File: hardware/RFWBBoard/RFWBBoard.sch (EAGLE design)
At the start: 8 parts, among them J1 CON-71742-2184-BOT, M1 MOUNT-HOLE3.3, M2 MOUNT-HOLE3.3, M3 MOUNT-HOLE3.3, M4 MOUNT-HOLE3.3, U1 MAX2830, U2 LDB212G4010C-001, U3 LDB212G4010C-001

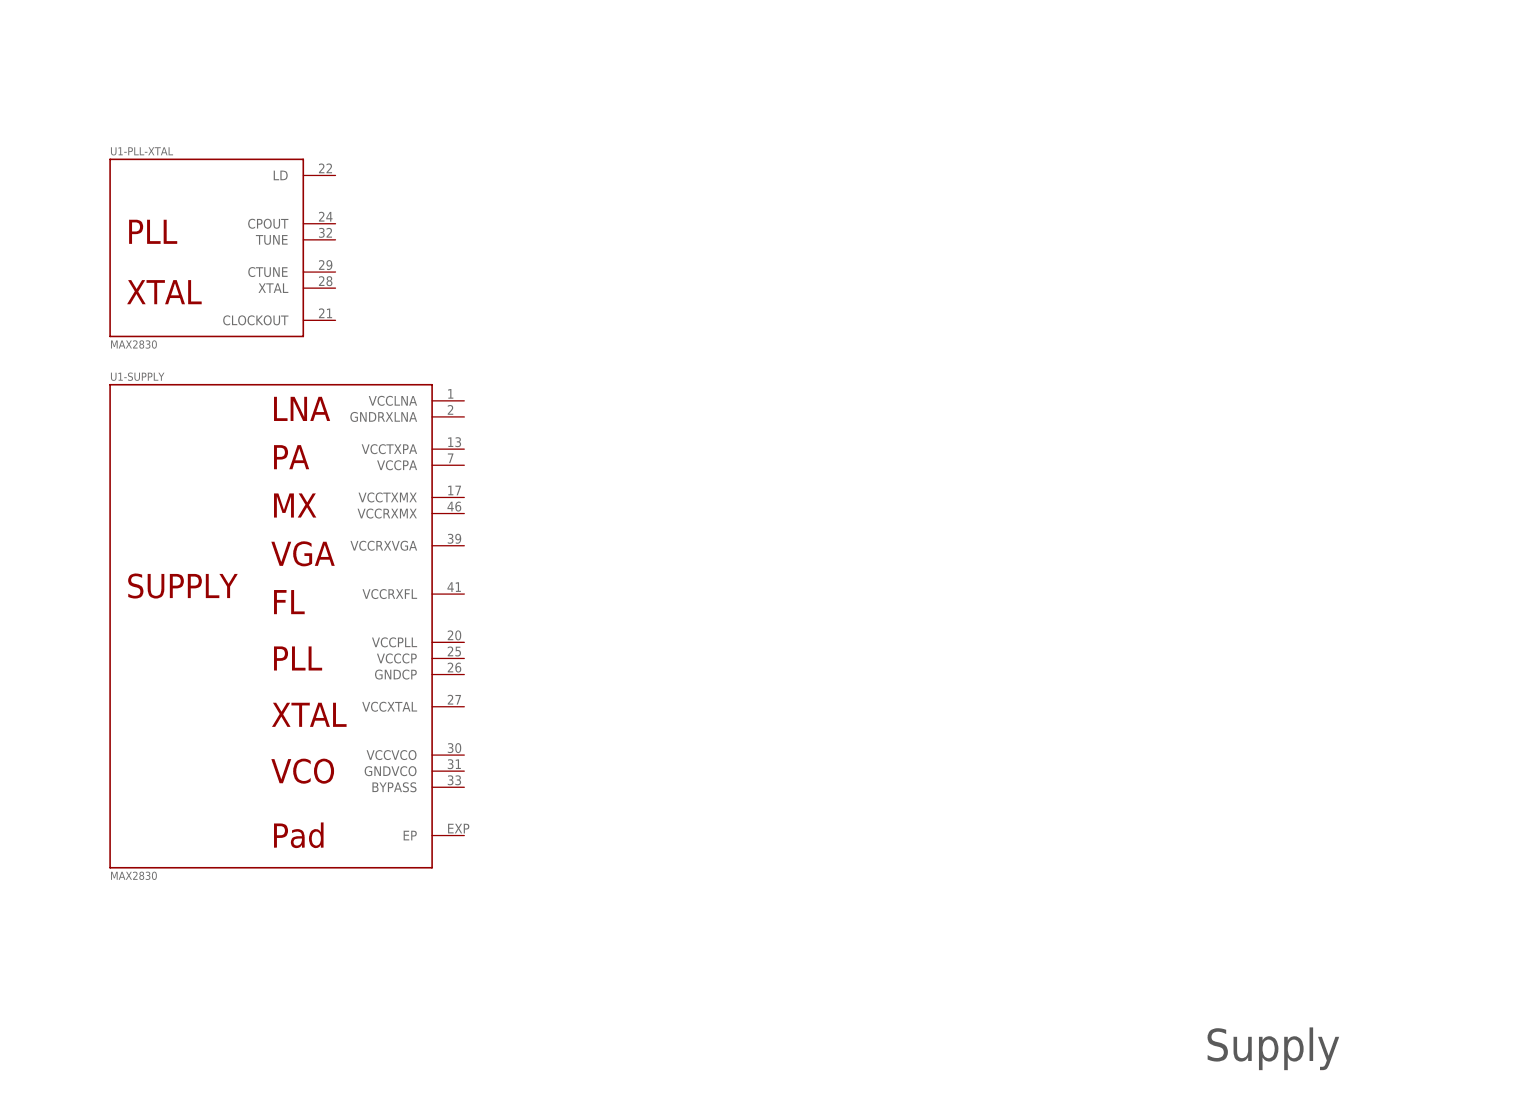
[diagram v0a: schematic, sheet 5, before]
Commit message: - 2.4 GHz Wide-Band Radio Front-End Board has most of the components
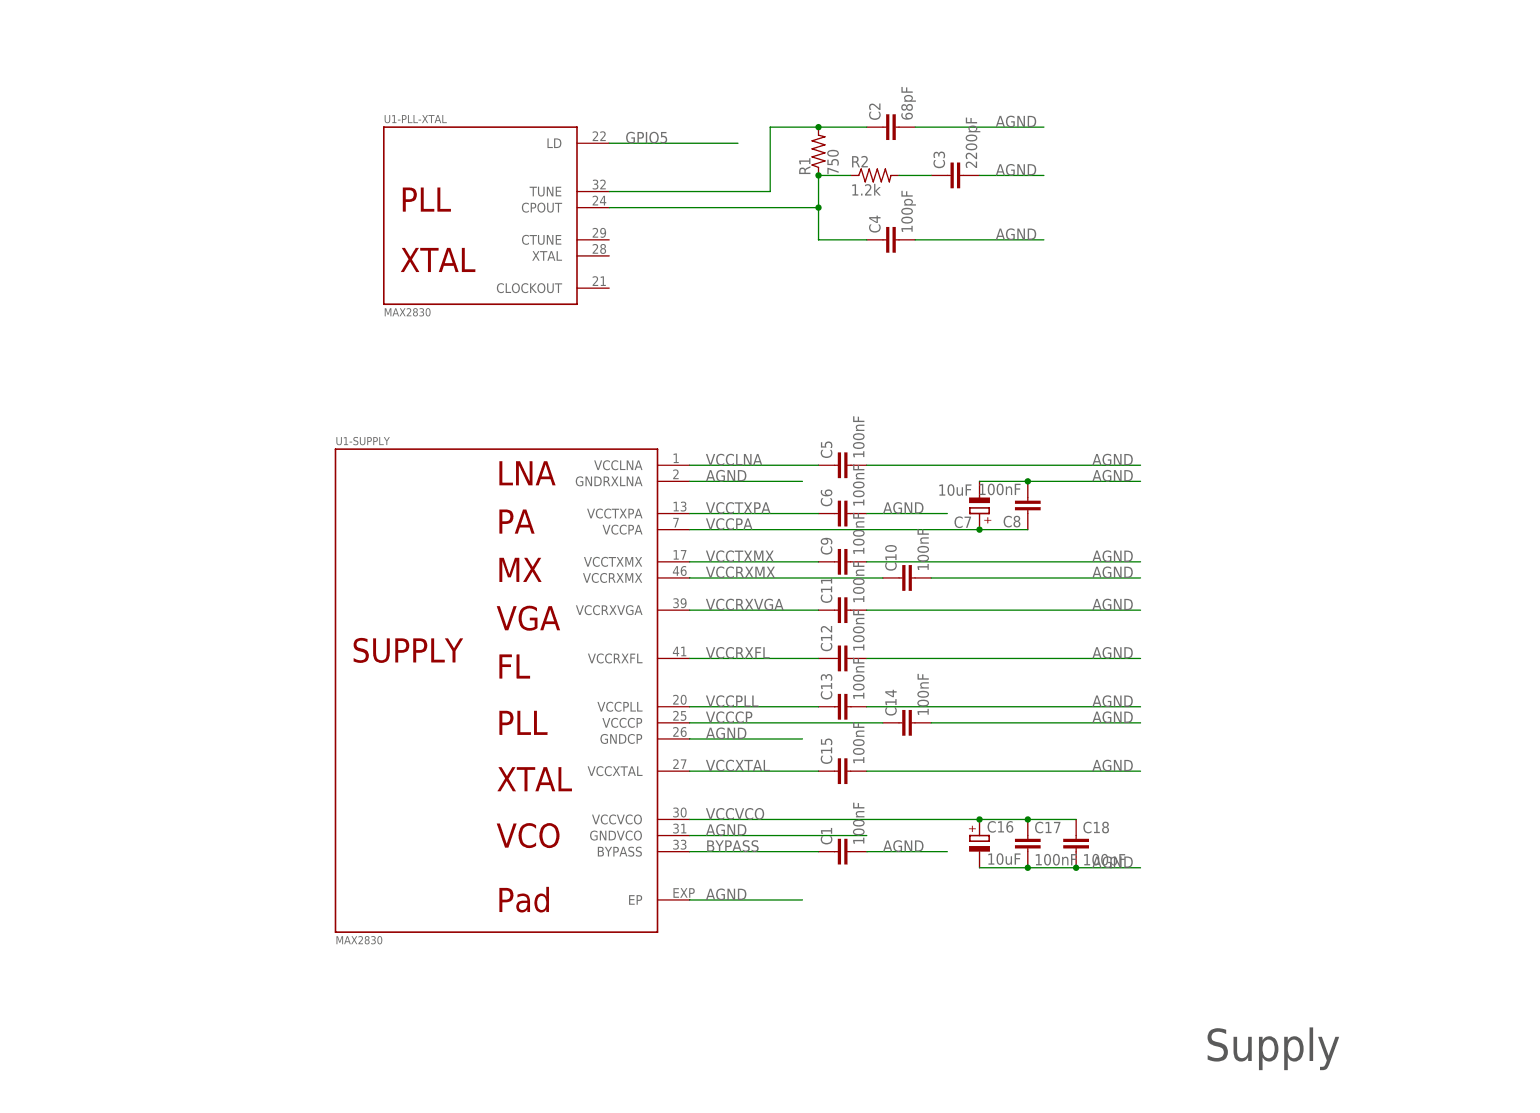
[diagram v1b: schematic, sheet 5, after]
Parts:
- added C1, C10, C11, C12, C13, C14, C15, C17, C5, C6, C8, C9: 100nF, RFWBBoard:C0402
- added C16, C7: 10uF, RFWBBoard:CPOL3216
- added C18, C4: 100pF, RFWBBoard:C0402
- added C2: 68pF, RFWBBoard:C0402
- added C3: 2200pF, RFWBBoard:C0402
- added R1: 750, RFWBBoard:R0402
- added R2: 1.2k, RFWBBoard:R0402
- added X1, X2: LTI-SASF54GT, RFWBBoard:LTI-SASF54GT
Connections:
- new net A1V5: J1.79, J1.80
- new net A3V3: J1.81, J1.82
- new net ADC1+: J1.71, U1-RX.RXBBQ+
- new net ADC1-: J1.73, U1-RX.RXBBQ-
- new net ADC2+: J1.65, U1-RX.RXBBI+
- new net ADC2-: J1.67, U1-RX.RXBBI-
- new net ADC3+: J1.47
- new net ADC3-: J1.49
- new net ADC4+: J1.41
- new net ADC4-: J1.43
- new net ADCSF1: J1.74, U1-CONTROL.RSSI
- new net ARESERVED: J1.77, J1.78
- new net BYPASS: C1.1, U1-SUPPLY.BYPASS
- new net D1V5: J1.7, J1.8
- new net D3V3: J1.5, J1.6
- new net DAC1+: J1.59, U1-TX.TXBBQ+
- new net DAC1-: J1.61, U1-TX.TXBBQ-
- new net DAC2+: J1.53, U1-TX.TXBBI+
- new net DAC2-: J1.55, U1-TX.TXBBI-
- new net DAC3+: J1.35
- new net DAC3-: J1.37
- new net DAC4+: J1.29
- new net DAC4-: J1.31
- new net DACSF1: J1.62
- new net DACSF2: J1.60
- new net DACSF3: J1.56
- new net DACSF4: J1.54
- new net DGND: J1.1, J1.11, J1.12, J1.2, J1.21
- new net DRESERVED: J1.10, J1.9
- new net GPIO1: J1.18, U1-CONTROL./SHDN
- new net GPIO2: J1.20, U1-CONTROL.RXTX
- new net GPIO3: J1.22, U1-CONTROL.ANTSEL
- new net GPIO4: J1.24, U1-CONTROL.RXHP
- new net GPIO5: J1.26, U1-PLL-XTAL.LD
- new net N$5: C2.1, R1.2, U1-PLL-XTAL.TUNE
- new net N$6: C4.1, R1.1, R2.1, U1-PLL-XTAL.CPOUT
- new net N$7: C3.1, R2.2
- new net N$8: U2.1, X1G$1.1
- new net N$9: U3.1, X2G$1.1
- new net SPI1_MOSI: J1.19, U1-SERIAL.DIN
- new net SPI1_NSS: J1.13, U1-SERIAL./CS
- new net SPI1_SCK: J1.15, U1-SERIAL.SCLK
- new net VCCCP: C14.1, U1-SUPPLY.VCCCP
- new net VCCLNA: C5.1, U1-SUPPLY.VCCLNA
- new net VCCPA: C7.+, C8.1, U1-SUPPLY.VCCPA
- new net VCCPLL: C13.1, U1-SUPPLY.VCCPLL
- new net VCCRXFL: C12.1, U1-SUPPLY.VCCRXFL
- new net VCCRXMX: C10.1, U1-SUPPLY.VCCRXMX
- new net VCCRXVGA: C11.1, U1-SUPPLY.VCCRXVGA
- new net VCCTXMX: C9.1, U1-SUPPLY.VCCTXMX
- new net VCCTXPA: C6.1, U1-SUPPLY.VCCTXPA
- new net VCCVCO: C16.+, C17.1, C18.1, U1-SUPPLY.VCCVCO
- new net VCCXTAL: C15.1, U1-SUPPLY.VCCXTAL
- new net VSUP: J1.3, J1.4
- net AGND: now also C1.2, C10.2, C11.2, C12.2, C13.2, C14.2, C15.2, C16.-, C17.2, C18.2, C2.2, C3.2, C4.2, C5.2, C6.2, C7.-, C8.2, C9.2, J1.27, J1.28, J1.33, J1.34, J1.39, J1.40, J1.45, J1.46, J1.51, J1.52, J1.57, J1.58, J1.63, J1.64, J1.69, J1.70, J1.75, J1.76, J1.83, J1.84, U1-SUPPLY.EP, U1-SUPPLY.GNDCP, U1-SUPPLY.GNDRXLNA, U1-SUPPLY.GNDVCO, X1G$1.GND, X1G.GND@1, X1G.GND@2, X1G.GND@3, X2G$1.GND, X2G.GND@1, X2G.GND@2, X2G.GND@3
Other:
- note added: "GAIN CONTROLLED"
- note added: "NOT USED,"
- note added: "THROUGH SPI"
- note added: "Wide-Band 2.4 GHz Radio Front-End for the Marmote platform"
- note removed: "Wide-Band Radio Front-End for the Marmote platform"
- moved on the sheet: U1-ANT, U1-CONTROL, U1-GAIN, U1-PLL-XTAL, U1-RX, U1-SERIAL, U1-SUPPLY, U1-TX, U2, U3

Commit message: - All caps for MAX2830 - Corrected 84-pin connector
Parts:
- removed C5, C8: 100nF, RFWBBoard:C0402
- removed C7: 10uF, RFWBBoard:CPOL3216
- added C61: 10uF, RFWBBoard:C1206
- added C78: 2200pF, RFWBBoard:C0402
- added C82: 10uF, RFWBBoard:C0805
- C16: value 10uF -> 100pF; device RFWBBoard:CPOL3216 -> RFWBBoard:C0402
- C3: value 2200pF -> 100pF
- C6: value 100nF -> NONE
- C70, C89: value 100nF -> 100pF
- C73, C74, C75, C87, C88: value 100nF -> 10nF
- renumbered C1 to C86, C10 to C89, C11 to C87, C12 to C88, C13 to C73, C14 to C74, C15 to C75, C17 to C83, C18 to C81, C2 to C80, C4 to C79, C9 to C70, R1 to R52, R2 to R51
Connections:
- net AGND: now also C16.2, C61.1, C78.2, C82.2; no longer C16.-, C5.2, C7.-, C8.2
- net N$7: now also C78.1; no longer C3.1
- net VCCLNA: now also C16.1; no longer C5.1
- net VCCPA: now also C3.1, C61.2; no longer C7.+, C8.1
- net VCCVCO: now also C82.1; no longer C16.+

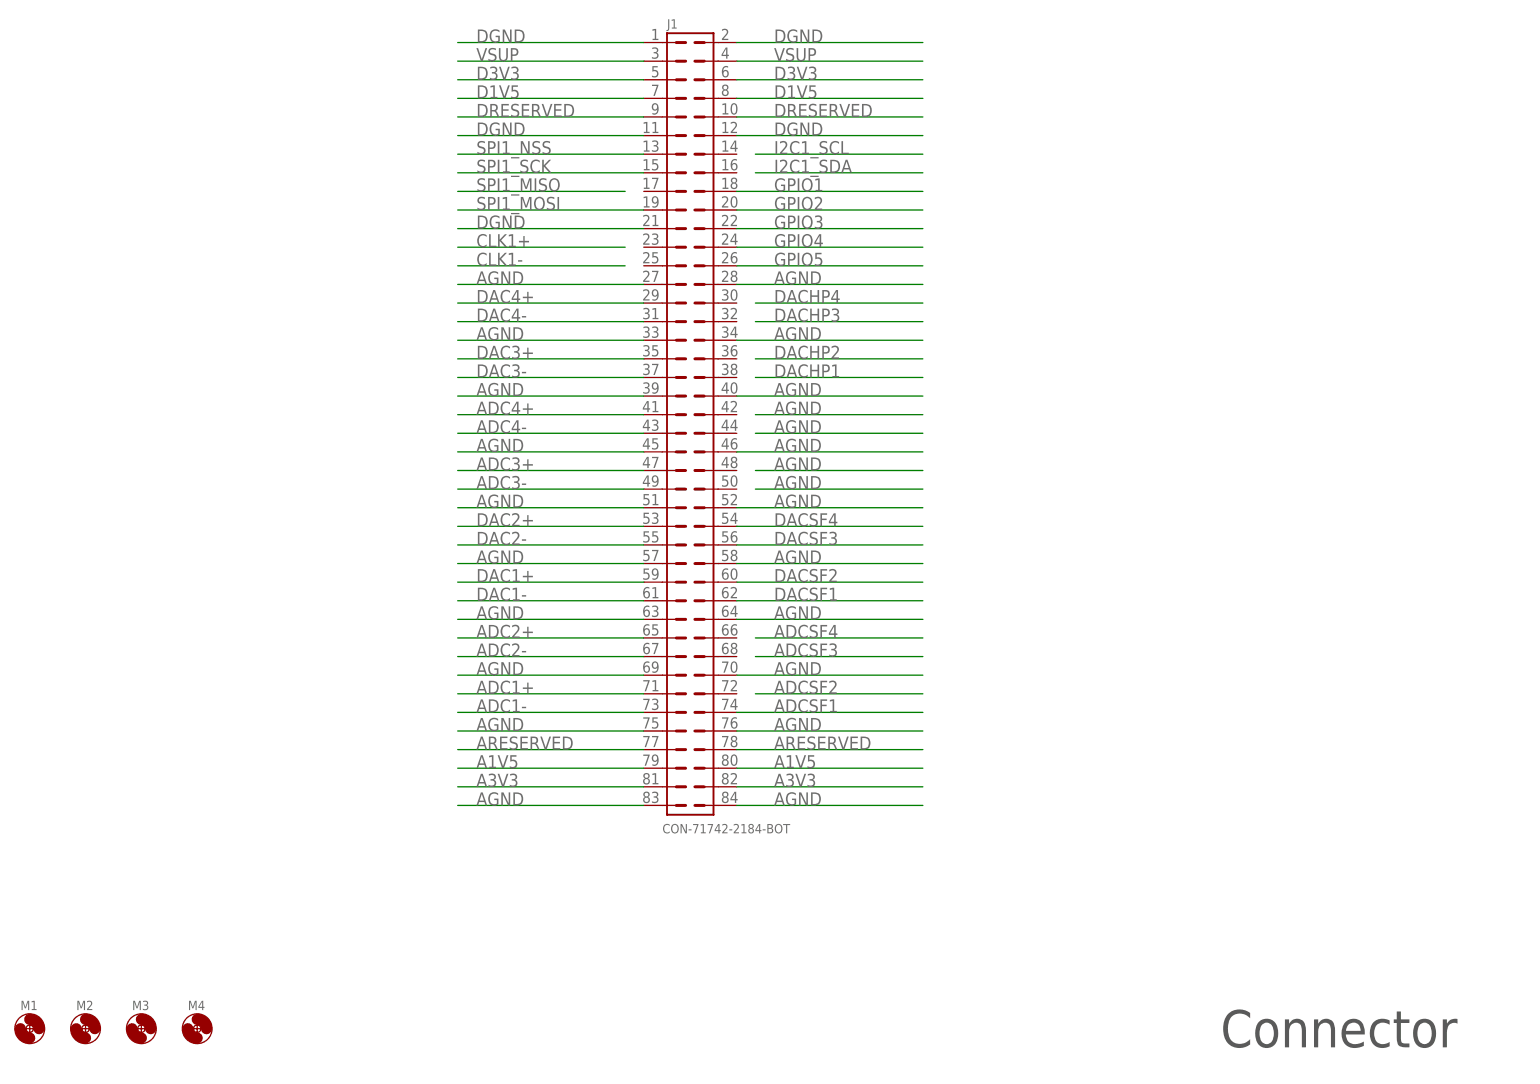
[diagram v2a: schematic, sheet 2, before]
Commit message: - RFWBboard layout changed
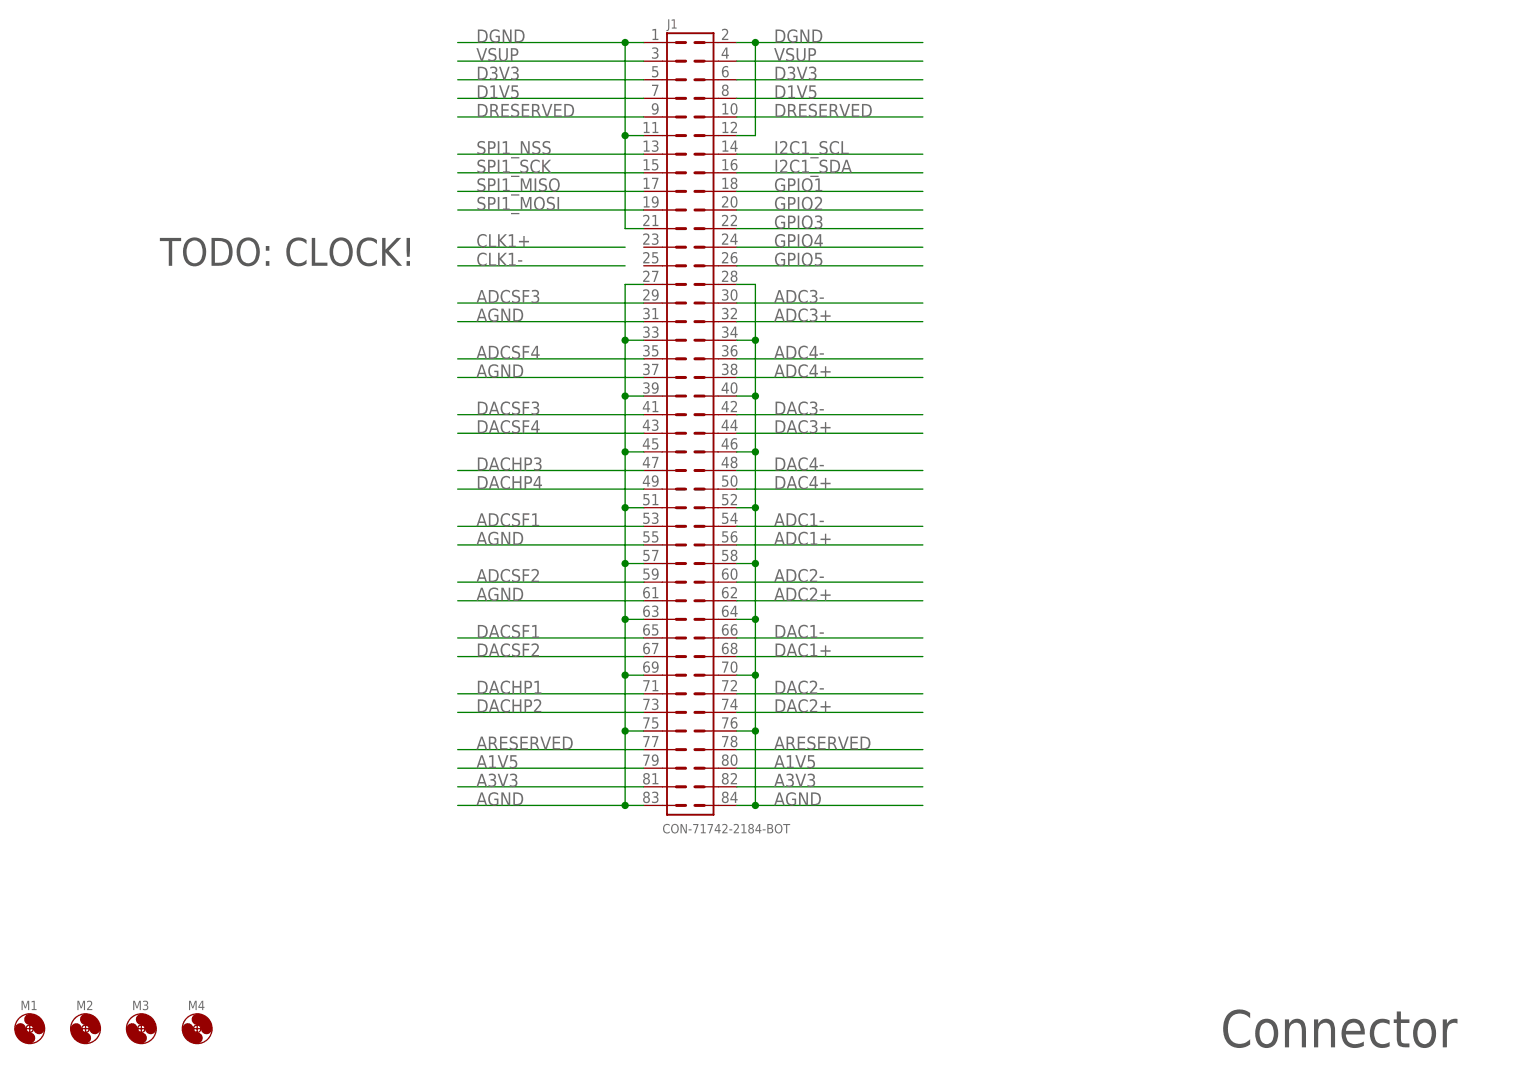
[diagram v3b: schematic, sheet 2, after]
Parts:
- added C66: 10uF, RFWBBoard:CPOL2012
- added C67: 100nF, RFWBBoard:C0402
- U1: value MAX2830 -> MAX2830IPC-7351; device RFWBBoard:MAX2830 -> RFWBBoard:MAX2830IPC-7351
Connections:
- removed net VCCCP: C74.1, U1-SUPPLY.VCCCP
- removed net VCCLNA: C16.1, U1-SUPPLY.VCCLNA
- removed net VCCPA: C3.1, C61.2, U1-SUPPLY.VCCPA
- removed net VCCPLL: C73.1, U1-SUPPLY.VCCPLL
- removed net VCCRXFL: C88.1, U1-SUPPLY.VCCRXFL
- removed net VCCRXMX: C89.1, U1-SUPPLY.VCCRXMX
- removed net VCCRXVGA: C87.1, U1-SUPPLY.VCCRXVGA
- removed net VCCTXMX: C70.1, U1-SUPPLY.VCCTXMX
- removed net VCCTXPA: C6.1, U1-SUPPLY.VCCTXPA
- removed net VCCVCO: C81.1, C82.1, C83.1, U1-SUPPLY.VCCVCO
- removed net VCCXTAL: C75.1, U1-SUPPLY.VCCXTAL
- new net ADCSF2: J1.59
- new net ADCSF3: J1.29
- new net ADCSF4: J1.35
- new net DACHP1: J1.71
- new net DACHP2: J1.73
- new net DACHP3: J1.47
- new net DACHP4: J1.49
- new net I2C1_SCL: J1.14
- new net I2C1_SDA: J1.16
- new net SPI1_MISO: J1.17
- net A3V3: now also C16.1, C3.1, C6.1, C61.2, C66.+, C67.1, C70.1, C73.1, C74.1, C75.1, C81.1, C82.1, C83.1, C87.1, C88.1, C89.1, U1-SUPPLY.VCCCP, U1-SUPPLY.VCCLNA, U1-SUPPLY.VCCPA, U1-SUPPLY.VCCPLL, U1-SUPPLY.VCCRXFL, U1-SUPPLY.VCCRXMX, U1-SUPPLY.VCCRXVGA, U1-SUPPLY.VCCTXMX, U1-SUPPLY.VCCTXPA, U1-SUPPLY.VCCVCO, U1-SUPPLY.VCCXTAL
- net ADC1+: now also J1.56; no longer J1.71
- net ADC1-: now also J1.54; no longer J1.73
- net ADC2+: now also J1.62; no longer J1.65
- net ADC2-: now also J1.60; no longer J1.67
- net ADC3+: now also J1.32; no longer J1.47
- net ADC3-: now also J1.30; no longer J1.49
- net ADC4+: now also J1.38; no longer J1.41
- net ADC4-: now also J1.36; no longer J1.43
- net ADCSF1: now also J1.53; no longer J1.74
- net AGND: now also C66.-, C67.2, J1.31, J1.37, J1.55, J1.61
- net DAC1+: now also J1.68; no longer J1.59
- net DAC1-: now also J1.66; no longer J1.61
- net DAC2+: now also J1.74; no longer J1.53
- net DAC2-: now also J1.72; no longer J1.55
- net DAC3+: now also J1.44; no longer J1.35
- net DAC3-: now also J1.42; no longer J1.37
- net DAC4+: now also J1.50; no longer J1.29
- net DAC4-: now also J1.48; no longer J1.31
- net DACSF1: now also J1.65; no longer J1.62
- net DACSF2: now also J1.67; no longer J1.60
- net DACSF3: now also J1.41; no longer J1.56
- net DACSF4: now also J1.43; no longer J1.54
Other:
- note added: "TODO: CLOCK!"
- note added: "TODO: CLOCK!!!"
- moved on the sheet: U1-SUPPLY
